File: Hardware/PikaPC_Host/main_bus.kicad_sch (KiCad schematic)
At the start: 5 parts, among them J2 DIN41612_03x32_C_Split, U2 ATF1508AS, U6 IDT74ALVC164245

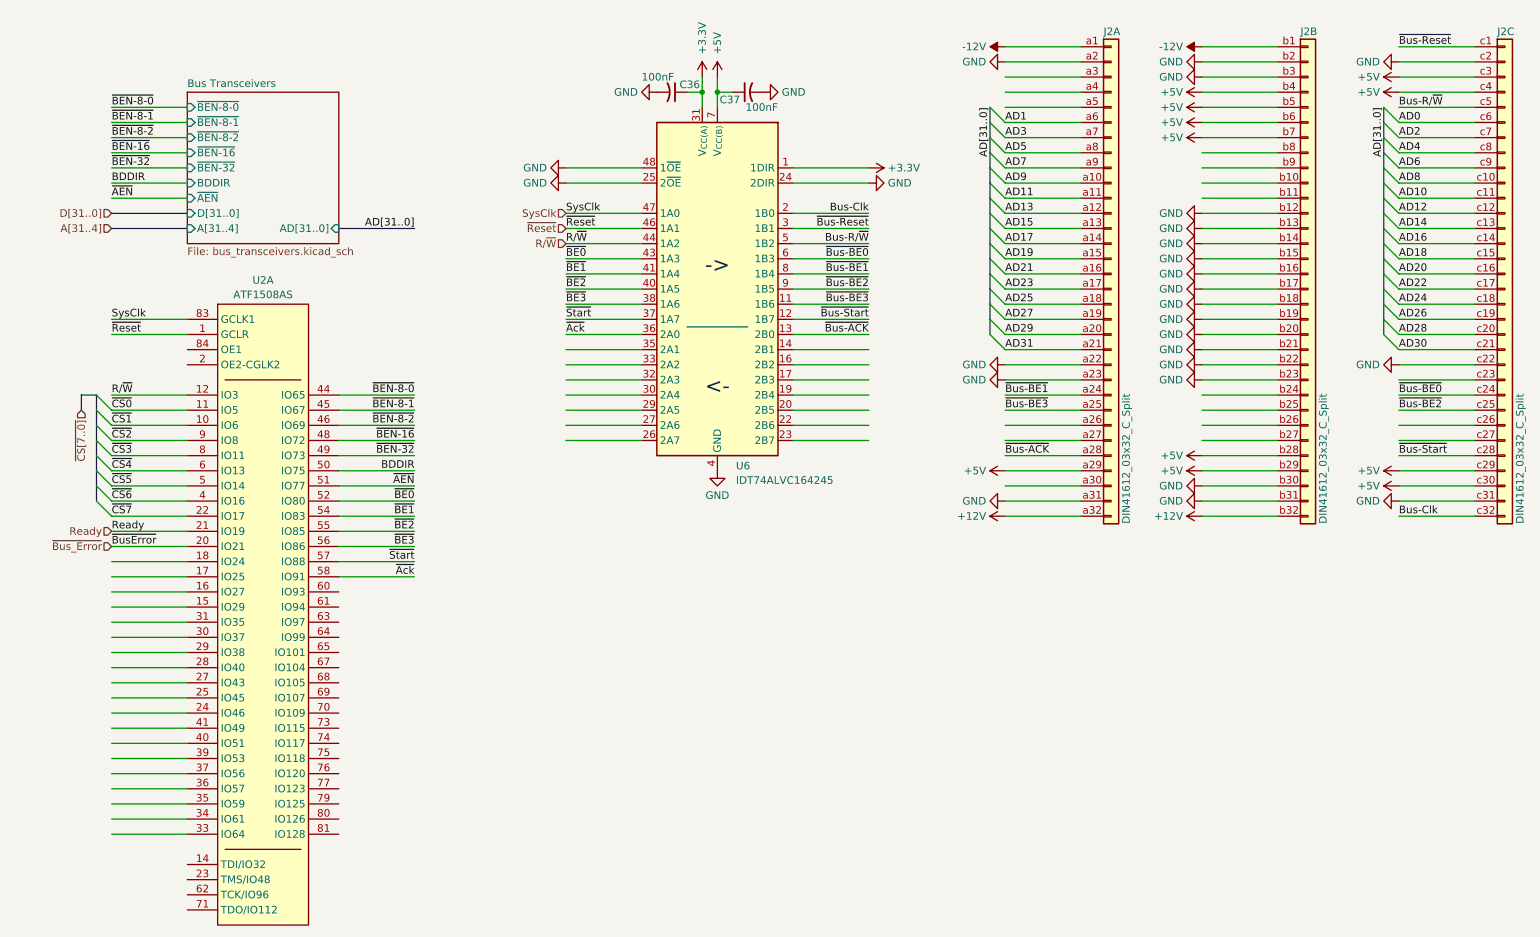
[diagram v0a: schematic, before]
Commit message: Host card PCB layout
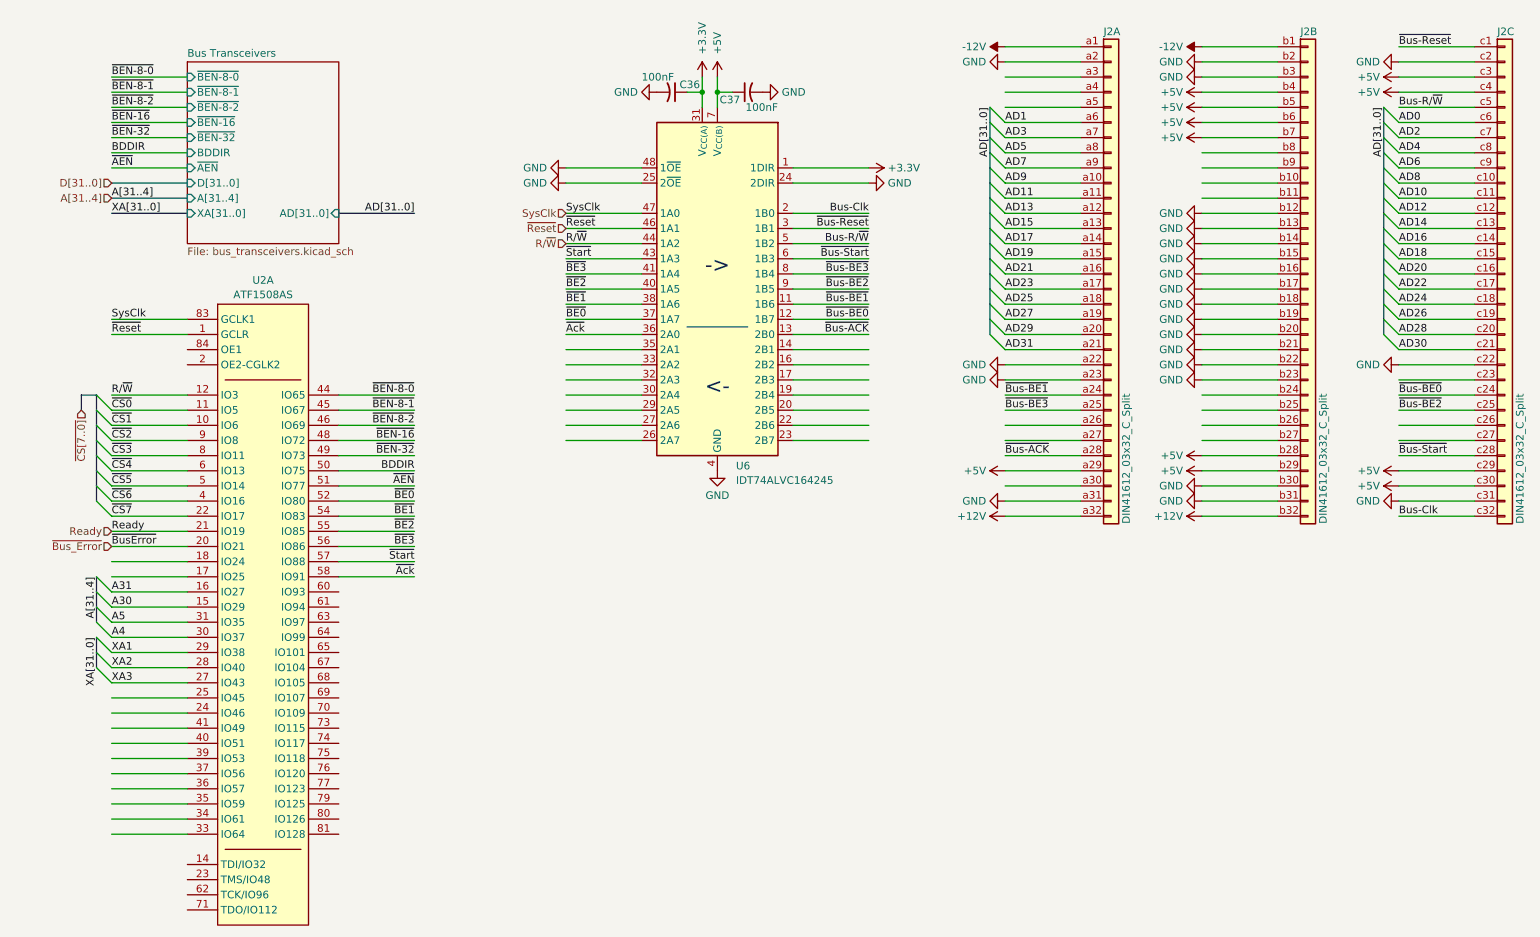
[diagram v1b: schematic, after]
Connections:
- net ~{BE0}: now also U6.37 (1A7); no longer U6.43 (1A3)
- net ~{BE1}: now also U6.38 (1A6); no longer U6.41 (1A4)
- net ~{BE3}: now also U6.41 (1A4); no longer U6.38 (1A6)
- net ~{Bus-BE0}: now also U6.12 (1B7); no longer U6.6 (1B3)
- net ~{Bus-BE1}: now also U6.11 (1B6); no longer U6.8 (1B4)
- net ~{Bus-BE3}: now also U6.8 (1B4); no longer U6.11 (1B6)
- net ~{Bus-Start}: now also U6.6 (1B3); no longer U6.12 (1B7)
- net ~{Start}: now also U6.43 (1A3); no longer U6.37 (1A7)
- net A30: now reaches U2.15 (IO29)
- net A31: now reaches U2.16 (IO27)
- net XA3: now reaches U2.27 (IO43)
- net XA2: now reaches U2.28 (IO40)
- net XA1: now reaches U2.29 (IO38)
- net A4: now reaches U2.30 (IO37)
- net A5: now reaches U2.31 (IO35)
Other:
- sheet Bus Transceivers ports: added XA[31..0]; removed none

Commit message: Host card PCB layout
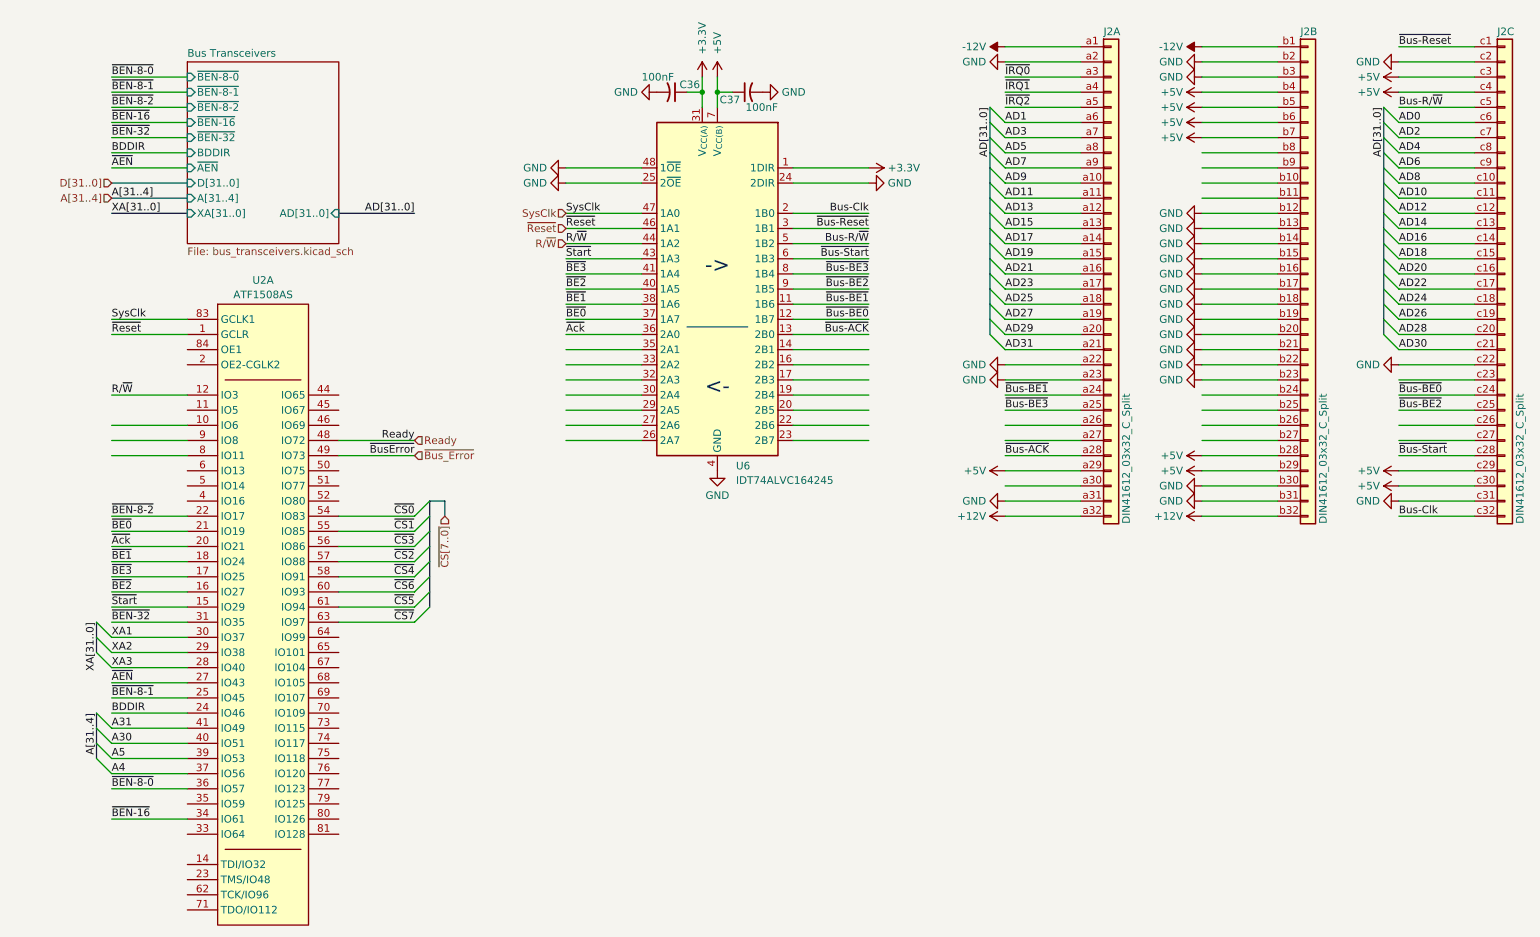
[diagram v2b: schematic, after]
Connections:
- net A30: now also U2.40 (IO51); no longer U2.15 (IO29)
- net A31: now also U2.41 (IO49); no longer U2.16 (IO27)
- net A4: now also U2.37 (IO56); no longer U2.30 (IO37)
- net A5: now also U2.39 (IO53); no longer U2.31 (IO35)
- net BDDIR: now also U2.24 (IO46); no longer U2.50 (IO75)
- net Ready: now also U2.48 (IO72); no longer U2.21 (IO19)
- net XA1: now also U2.30 (IO37); no longer U2.29 (IO38)
- net XA2: now also U2.29 (IO38); no longer U2.28 (IO40)
- net XA3: now also U2.28 (IO40); no longer U2.27 (IO43)
- net ~{AEN}: now also U2.27 (IO43); no longer U2.51 (IO77)
- net ~{Ack}: now also U2.20 (IO21); no longer U2.58 (IO91)
- net ~{BE0}: now also U2.21 (IO19); no longer U2.52 (IO80)
- net ~{BE1}: now also U2.18 (IO24); no longer U2.54 (IO83)
- net ~{BE2}: now also U2.16 (IO27); no longer U2.55 (IO85)
- net ~{BE3}: now also U2.17 (IO25); no longer U2.56 (IO86)
- net ~{BEN-16}: now also U2.34 (IO61); no longer U2.48 (IO72)
- net ~{BEN-32}: now also U2.31 (IO35); no longer U2.49 (IO73)
- net ~{BEN-8-0}: now also U2.36 (IO57); no longer U2.44 (IO65)
- net ~{BEN-8-1}: now also U2.25 (IO45); no longer U2.45 (IO67)
- net ~{BEN-8-2}: now also U2.22 (IO17); no longer U2.46 (IO69)
- net ~{Bus_Error}: now also U2.49 (IO73); no longer U2.20 (IO21)
- net ~{CS0}: now also U2.54 (IO83); no longer U2.11 (IO5)
- net ~{CS1}: now also U2.55 (IO85); no longer U2.10 (IO6)
- net ~{CS2}: now also U2.57 (IO88); no longer U2.9 (IO8)
- net ~{CS3}: now also U2.56 (IO86); no longer U2.8 (IO11)
- net ~{CS4}: now also U2.58 (IO91); no longer U2.6 (IO13)
- net ~{CS5}: now also U2.61 (IO94); no longer U2.5 (IO14)
- net ~{CS6}: now also U2.60 (IO93); no longer U2.4 (IO16)
- net ~{CS7}: now also U2.63 (IO97); no longer U2.22 (IO17)
- net ~{Start}: now also U2.15 (IO29); no longer U2.57 (IO88)
- net ~{IRQ0}: now reaches J2.a3 (Pin_a3)
- net ~{IRQ1}: now reaches J2.a4 (Pin_a4)
- net ~{IRQ2}: now reaches J2.a5 (Pin_a5)

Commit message: Rework bus pinout
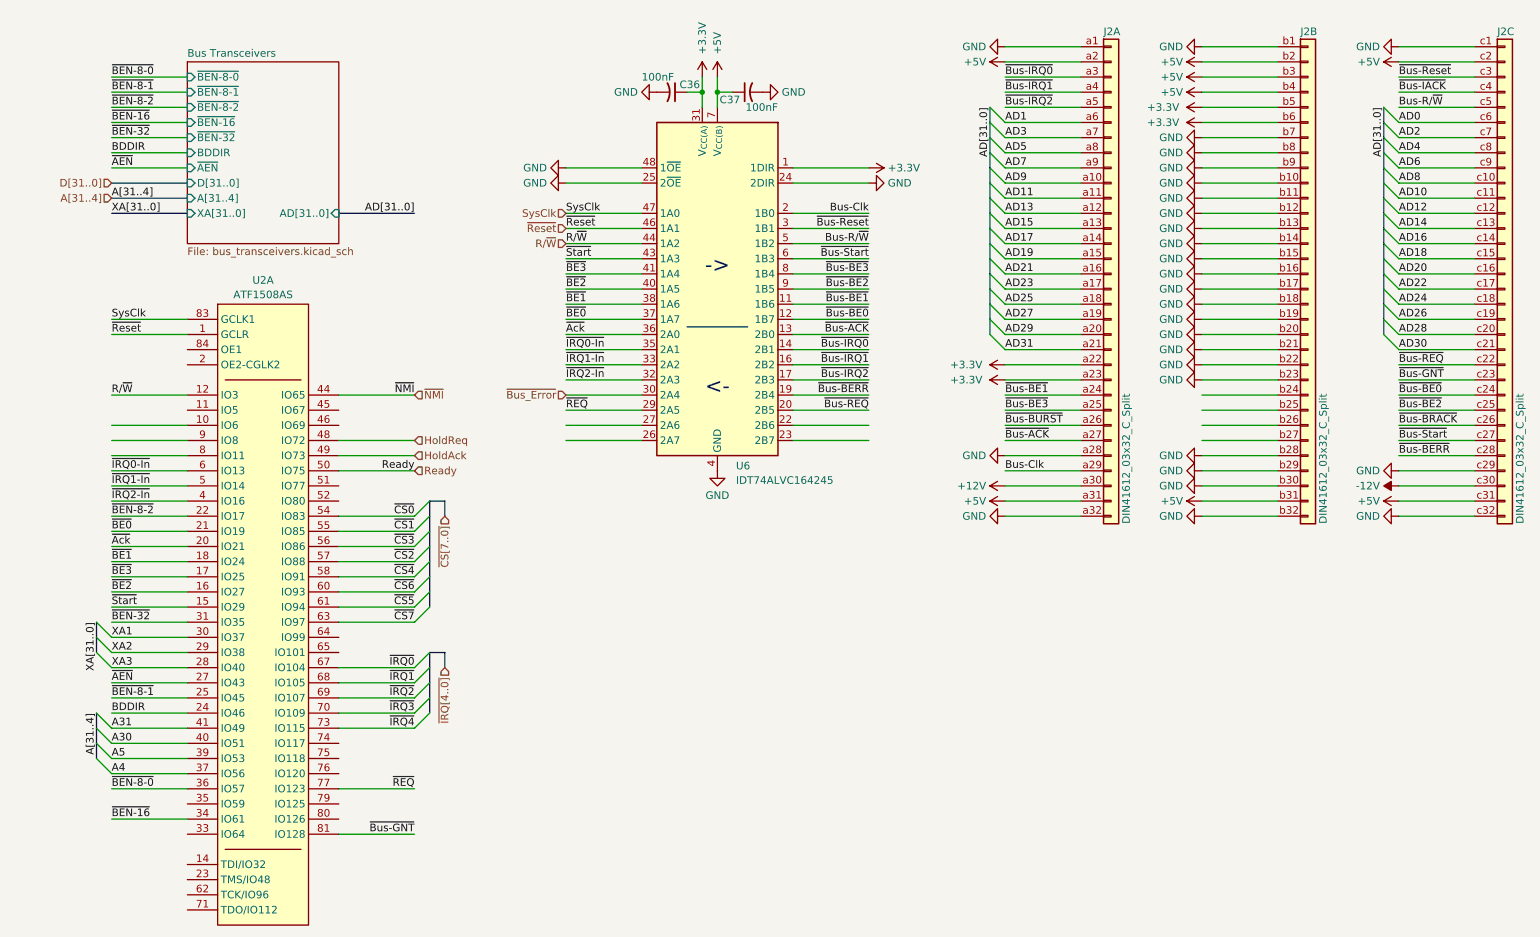
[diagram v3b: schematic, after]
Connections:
- net +12V: now also J2.a30 (Pin_a30); no longer J2.a32 (Pin_a32), J2.b32 (Pin_b32)
- net +3.3V: now also J2.a22 (Pin_a22), J2.a23 (Pin_a23), J2.b5 (Pin_b5), J2.b6 (Pin_b6)
- net +5V: now also J2.a2 (Pin_a2), J2.a31 (Pin_a31), J2.b2 (Pin_b2), J2.b3 (Pin_b3), J2.b31 (Pin_b31), J2.c2 (Pin_c2), J2.c31 (Pin_c31); no longer J2.a29 (Pin_a29), J2.b28 (Pin_b28), J2.b29 (Pin_b29), J2.b5 (Pin_b5), J2.b6 (Pin_b6), J2.b7 (Pin_b7), J2.c29 (Pin_c29), J2.c3 (Pin_c3), J2.c30 (Pin_c30), J2.c4 (Pin_c4)
- net -12V: now also J2.c30 (Pin_c30); no longer J2.a1 (Pin_a1), J2.b1 (Pin_b1)
- net Bus-Clk: now also J2.a29 (Pin_a29); no longer J2.c32 (Pin_c32)
- net GND: now also J2.a1 (Pin_a1), J2.a28 (Pin_a28), J2.a32 (Pin_a32), J2.b1 (Pin_b1), J2.b10 (Pin_b10), J2.b11 (Pin_b11), J2.b28 (Pin_b28), J2.b29 (Pin_b29), J2.b32 (Pin_b32), J2.b7 (Pin_b7), J2.b8 (Pin_b8), J2.b9 (Pin_b9), J2.c1 (Pin_c1), J2.c29 (Pin_c29), J2.c32 (Pin_c32); no longer J2.a2 (Pin_a2), J2.a22 (Pin_a22), J2.a23 (Pin_a23), J2.a31 (Pin_a31), J2.b2 (Pin_b2), J2.b3 (Pin_b3), J2.b31 (Pin_b31), J2.c2 (Pin_c2), J2.c22 (Pin_c22), J2.c31 (Pin_c31)
- net Ready: now also U2.50 (IO75); no longer U2.48 (IO72)
- net ~{Bus-ACK}: now also J2.a27 (Pin_a27); no longer J2.a28 (Pin_a28)
- net ~{Bus-Reset}: now also J2.c3 (Pin_c3); no longer J2.c1 (Pin_c1)
- net ~{Bus-Start}: now also J2.c27 (Pin_c27); no longer J2.c28 (Pin_c28)
- net ~{Bus_Error}: now also U6.30 (2A4); no longer U2.49 (IO73)
- net ~{IRQ0}: now also U2.67 (IO104); no longer J2.a3 (Pin_a3)
- net ~{IRQ1}: now also U2.68 (IO105); no longer J2.a4 (Pin_a4)
- net ~{IRQ2}: now also U2.69 (IO107); no longer J2.a5 (Pin_a5)
- net ~{Bus-GNT}: now reaches J2.c23 (Pin_c23)
- net ~{Bus-GNT}: now also U2.81 (IO128)
- net ~{Bus-BRACK}: now reaches J2.c26 (Pin_c26)
- net ~{IRQ2-In}: now reaches U2.4 (IO16)
- net ~{IRQ2-In}: now also U6.32 (2A3)
- net ~{NMI}: now reaches U2.44 (IO65)
- net ~{IRQ1-In}: now reaches U2.5 (IO14)
- net ~{IRQ1-In}: now also U6.33 (2A2)
- net ~{IRQ0-In}: now reaches U2.6 (IO13)
- net ~{IRQ0-In}: now also U6.35 (2A1)
- net ~{IRQ3}: now reaches U2.70 (IO109)
- net ~{IRQ4}: now reaches U2.73 (IO115)
- net ~{REQ}: now reaches U2.77 (IO123)
- net ~{REQ}: now also U6.29 (2A5)
- net ~{Bus-IRQ0}: now reaches U6.14 (2B1)
- net ~{Bus-IRQ0}: now also J2.a3 (Pin_a3)
- net ~{Bus-IRQ1}: now reaches U6.16 (2B2)
- net ~{Bus-IRQ1}: now also J2.a4 (Pin_a4)
- net ~{Bus-IRQ2}: now reaches U6.17 (2B3)
- net ~{Bus-IRQ2}: now also J2.a5 (Pin_a5)
- net ~{Bus-BERR}: now reaches U6.19 (2B4)
- net ~{Bus-BERR}: now also J2.c28 (Pin_c28)
- net ~{Bus-REQ}: now reaches U6.20 (2B5)
- net ~{Bus-REQ}: now also J2.c22 (Pin_c22)
- net ~{Bus-BURST}: now reaches J2.a26 (Pin_a26)
- new net HoldAck: U2.49 (IO73)
- new net HoldReq: U2.48 (IO72)
- new net ~{Bus-IACK}: J2.c4 (Pin_c4)

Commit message: ViRGE card PCB layout
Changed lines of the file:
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@@
-	(wire
-		(pts
-			(xy 25.4 83.82) (xy 38.1 83.82)
-		)
-		(stroke
-			(width 0)
-			(type default)
-		)
-	)
 	(wire
 		(pts
@@
 		)
 	)
-	(wire
-		(pts
-			(xy 25.4 86.36) (xy 38.1 86.36)
-		)
-		(stroke
-			(width 0)
-			(type default)
-		)
-	)
 	(bus
 		(pts
@@
 		)
 		(stroke
-			(width 0)
-			(type default)
-		)
-	)
-	(wire
-		(pts
-			(xy 25.4 81.28) (xy 38.1 81.28)
-		)
-		(stroke

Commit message: Host Card refinement
add main bus clock selection
silkscreen cleanup
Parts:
- added J3: Conn_01x03, Connector_PinHeader_2.54mm:PinHeader_1x03_P2.54mm_Vertical, symbol Connector_Generic:Conn_01x03
- U6: value IDT74ALVC164245 -> 74ALVC164245
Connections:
- net BusClkDiv3: now reaches U2.45 (IO67)
- net BusClkDiv3: now also J3.3 (Pin_3)
- net CpuClk: now reaches U6.23 (2B7)
- net CpuClk3: now reaches U6.26 (2A7)
- net CpuClk3: now also U2.83 (GCLK1), J3.1 (Pin_1)
- net SysClk renamed BusClk3
- net BusClk3: now also J3.2 (Pin_2); no longer U2.83 (GCLK1)
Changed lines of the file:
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@@
 		)
 	)
+	(wire
+		(pts
+			(xy 114.3 111.76) (xy 127 111.76)
+		)
+		(stroke
+			(width 0)
+			(type default)
+		)
+	)
 	(bus
 		(pts
@@
 	(wire
 		(pts
+			(xy 63.5 78.74) (xy 76.2 78.74)
+		)
+		(stroke
+			(width 0)
+			(type default)
+		)
+	)
+	(wire
+		(pts
 			(xy 208.28 76.2) (xy 220.98 76.2)
 		)
@@
 	(wire
 		(pts
+			(xy 114.3 114.3) (xy 127 114.3)
+		)
+		(stroke
+			(width 0)
+			(type default)
+		)
+	)
+	(wire
+		(pts
 			(xy 38.1 109.22) (xy 25.4 109.22)
 		)
@@
 	(wire
 		(pts
+			(xy 127 116.84) (xy 114.3 116.84)
+		)
+		(stroke
+			(width 0)
+			(type default)
+		)
+	)
+	(wire
+		(pts
 			(xy 25.4 127) (xy 38.1 127)
 		)
@@
 		)
 	)
-	(label "SysClk"
-		(at 101.6 45.72 0)
-		(effects
-			(font
-				(size 1.27 1.27)
-			)
-			(justify left bottom)
-		)
-	)
 	(label "AD9"
 		(at 175.26 40.64 0)
@@
 		)
 	)
+	(label "CpuClk3"
+		(at 25.4 63.5 0)
+		(effects
+			(font
+				(size 1.27 1.27)
+			)
+			(justify left bottom)
+		)
+	)
 	(label "Ready"
 		(at 76.2 88.9 180)
@@
 		)
 	)
+	(label "CpuClk3"
+		(at 101.6 83.82 0)
+		(effects
+			(font
+				(size 1.27 1.27)
+			)
+			(justify left bottom)
+		)
+	)
 	(label "~{AEN}"
 		(at 25.4 38.1 0)
@@
 		)
 	)
-	(label "SysClk"
-		(at 25.4 63.5 0)
+	(label "CpuClk"
+		(at 152.4 83.82 180)
 		(effects
 			(font
 				(size 1.27 1.27)
 			)
-			(justify left bottom)
+			(justify right bottom)
 		)
 	)
@@
 		)
 	)
+	(label "BusClkDiv3"
+		(at 114.3 116.84 0)
+		(effects
+			(font
+				(size 1.27 1.27)
+			)
+			(justify left bottom)
+		)
+	)
 	(label "~{CS7}"
 		(at 76.2 114.3 180)
@@
 		)
 	)
+	(label "CpuClk3"
+		(at 114.3 111.76 0)
+		(effects
+			(font
+				(size 1.27 1.27)
+			)
+			(justify left bottom)
+		)
+	)
 	(label "~{BEN-32}"
 		(at 25.4 114.3 0)
@@
 		)
 	)
+	(label "BusClkDiv3"
+		(at 76.2 78.74 180)
+		(effects
+			(font
+				(size 1.27 1.27)
+			)
+			(justify right bottom)
+		)
+	)
 	(label "BDDIR"
 		(at 25.4 35.56 0)
@@
 		)
 	)
+	(label "BusClk3"
+		(at 101.6 45.72 0)
+		(effects
+			(font
+				(size 1.27 1.27)
+			)
+			(justify left bottom)
+		)
+	)
 	(label "~{Bus-Reset}"
 		(at 152.4 48.26 180)
@@
 		)
 	)
+	(label "BusClk3"
+		(at 114.3 114.3 0)
+		(effects
+			(font
+				(size 1.27 1.27)
+			)
+			(justify left bottom)
+		)
+	)
 	(label "~{BE0}"
 		(at 101.6 63.5 0)
@@
 		)
 	)
-	(hierarchical_label "SysClk"
+	(hierarchical_label "CpuClk"
 		(shape input)
-		(at 101.6 45.72 180)
+		(at 152.4 83.82 0)
 		(effects
 			(font
 				(size 1.27 1.27)
 			)
-			(justify right)
+			(justify left)
 		)
 	)
@@
 	)
 	(symbol
+		(lib_id "Connector_Generic:Conn_01x03")
+		(at 132.08 114.3 0)
+		(unit 1)
+		(exclude_from_sim no)
+		(in_bom yes)
+		(on_board yes)
+		(dnp no)
+		(fields_autoplaced yes)
+		(property "Reference" "J3"
+			(at 134.112 113.0878 0)
+			(effects
+				(font
+					(size 1.27 1.27)
+				)
+				(justify left)
+			)
+		)
+		(property "Value" "Conn_01x03"
+			(at 134.112 115.5121 0)
+			(effects
+				(font
+					(size 1.27 1.27)
+				)
+				(justify left)
+			)
+		)
+		(property "Footprint" "Connector_PinHeader_2.54mm:PinHeader_1x03_P2.54mm_Vertical"
+			(at 132.08 114.3 0)
+			(effects
+				(font
+					(size 1.27 1.27)
+				)
+				(hide yes)
+			)
+		)
+		(property "Datasheet" "~"
+			(at 132.08 114.3 0)
+			(effects
+				(font
+					(size 1.27 1.27)
+				)
+				(hide yes)
+			)
+		)
+		(property "Description" "Generic connector, single row, 01x03, script generated (kicad-library-utils/schlib/autogen/connector/)"
+			(at 132.08 114.3 0)
+			(effects
+				(font
+					(size 1.27 1.27)
+				)
+				(hide yes)
+			)
+		)
+		(pin "3"
+		)
+		(pin "1"
+		)
+		(pin "2"
+		)
+		(instances
+			(project ""
+				(path "/6a60ec03-e28d-46ba-8906-3c4e1028fc94/541b8728-35ef-42a9-8317-6c507b38c6a8"
+					(reference "J3")
+					(unit 1)
+				)
+			)
+		)
+	)
+	(symbol
 		(lib_id "power:+5V")
 		(at 241.3 93.98 90)
@@
 			)
 		)
-		(property "Value" "IDT74ALVC164245"
+		(property "Value" "74ALVC164245"
 			(at 130.1181 90.5044 0)
 			(effects
